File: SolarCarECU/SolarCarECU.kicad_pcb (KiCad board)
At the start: 4 copper layers, 160 x 100 mm, 116 parts, among them J1 Screw_Terminal_01x02, J2 USB_B_Micro, J3 Screw_Terminal_01x05, J4 Screw_Terminal_01x08, J5 Screw_Terminal_01x08, J6 Screw_Terminal_01x14, J7 Screw_Terminal_01x14, Q1 QM6015D, Q2 PZT2222A, Q3 QM6015D, Q4 QM6015D, Q5 QM6015D, Q6 QM6015D, U1 Teensy3.6, U10 LM324A, U2 EL7202CN, U3 EL7202CN, U4 L7805, U5 MCP2562-E-P, U6 MCP2562-E-P, U7 4504, U8 4504, U9 4504

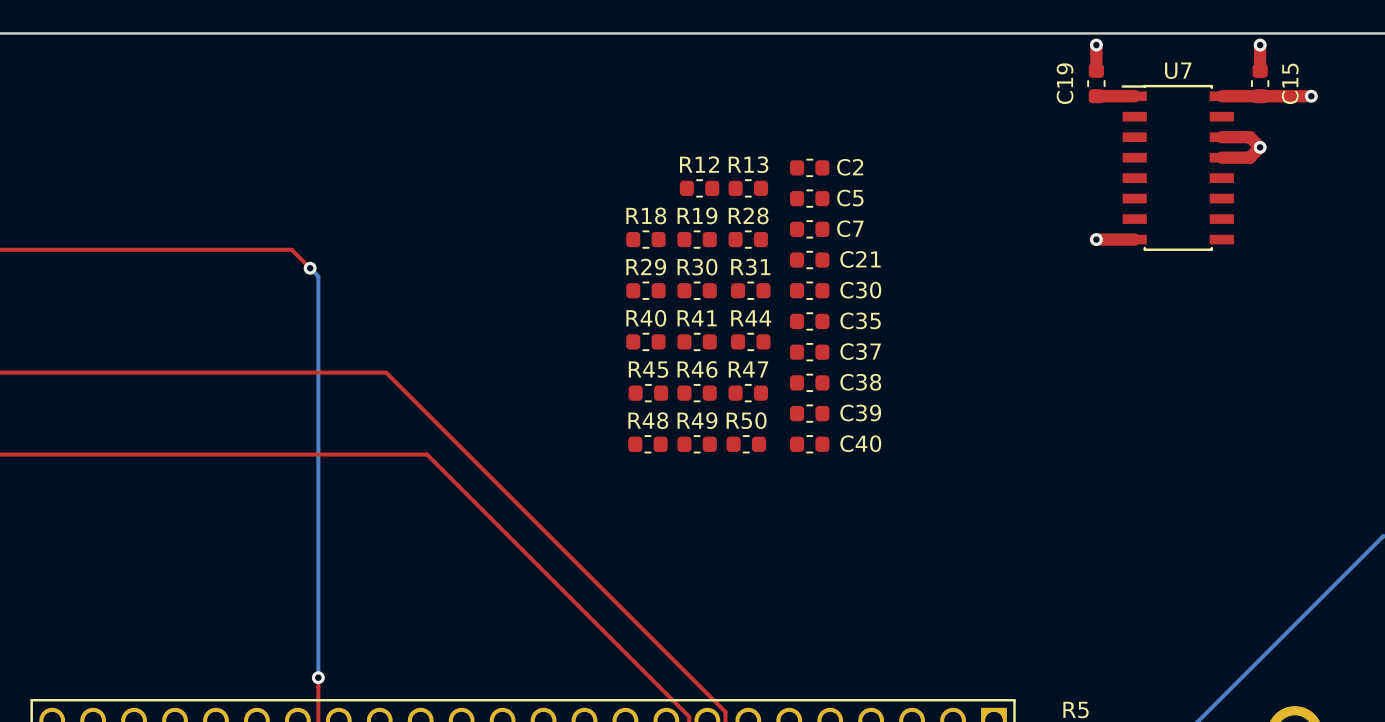
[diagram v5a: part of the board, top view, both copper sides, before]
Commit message: added logos
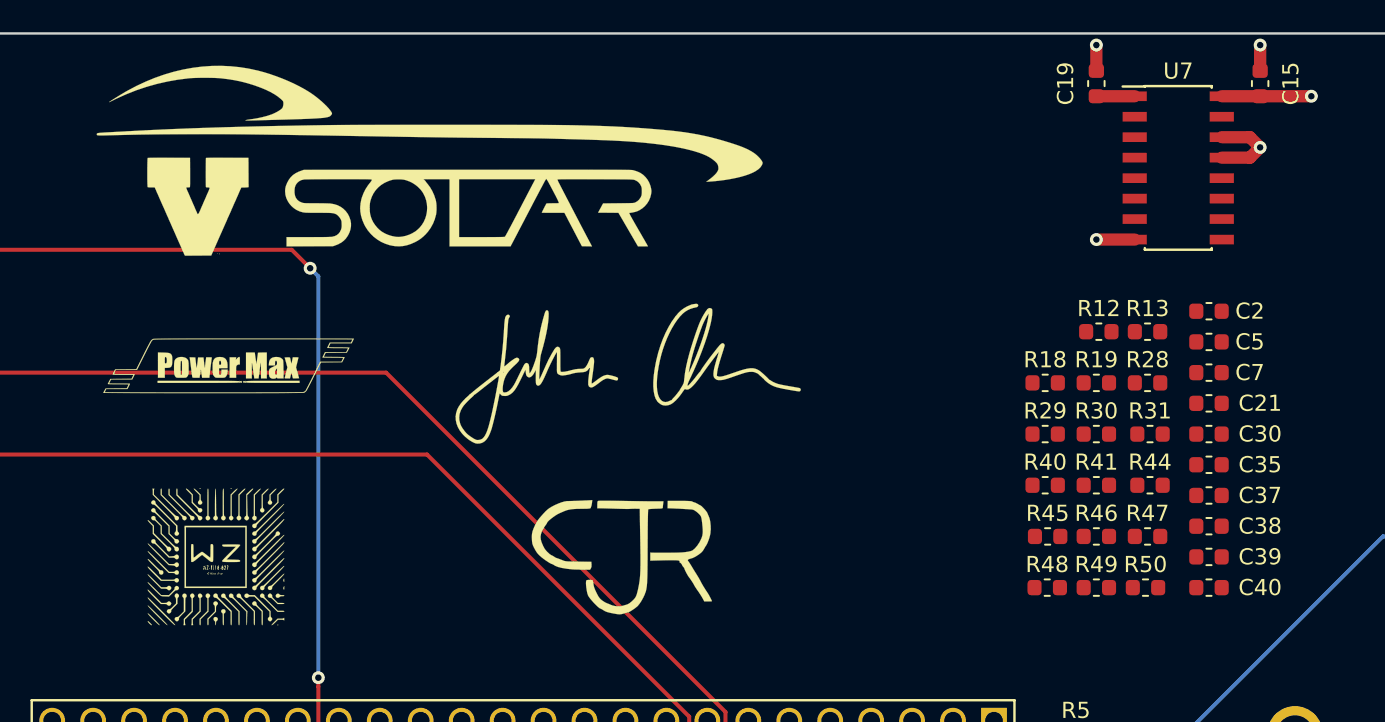
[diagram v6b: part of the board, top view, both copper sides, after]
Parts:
- added G***: LOGO, logo:SOLAR, F.Cu at (181.0, 52.7)
- added G***: LOGO, logo:PowerMax, F.Cu at (168.3, 65.4)
- added G***: LOGO, logo:WZ, F.Cu at (167.6, 77.5)
- added G***: LOGO, logo:CJR, F.Cu at (193.0, 77.5)
- added G***: LOGO, logo:JohnC, F.Cu at (192.4, 66.0)
- moved C37 26.3 mm to (229.2, 73.7)
- moved C38 26.3 mm to (229.2, 75.6)
- moved C39 26.3 mm to (229.2, 77.5)
- moved C40 26.3 mm to (229.2, 79.4)
- moved C5 26.3 mm to (229.2, 64.1)
- moved C7 26.3 mm to (229.2, 66.0)
- moved R12 26.3 mm to (222.4, 63.5)
- moved R13 26.3 mm to (225.4, 63.5)
- moved R28 26.3 mm to (225.4, 66.7)
- moved R47 26.3 mm to (225.4, 76.2)
- moved R50 26.3 mm to (225.3, 79.4)
- moved C2 26.3 mm to (229.2, 62.2)
- moved C21 26.3 mm to (229.2, 67.9)
- moved C30 26.3 mm to (229.2, 69.8)
- moved C35 26.3 mm to (229.2, 71.8)
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
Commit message: Wiring
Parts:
- moved R44 129.6 mm to (96.5, 84.5)
- moved R47 126.2 mm to (99.7, 87.0)
- moved R46 126.2 mm to (96.5, 87.0)
- moved R45 119.8 mm to (99.7, 84.5)
- moved C2 113.9 mm to (115.6, 70.2)
- moved C5 113.8 mm to (115.6, 68.6)
- moved C7 113.7 mm to (115.6, 67.0)
- moved R50 111.7 mm to (115.4, 59.1)
- moved R49 107.6 mm to (115.6, 65.4)
- moved R48 103.9 mm to (115.6, 71.8)
- moved C38 53.7 mm to (185.4, 106.7), turned to 270 degrees
- moved C37 52.9 mm to (188.0, 106.7), turned to 270 degrees
- moved C35 52.2 mm to (190.5, 106.7), turned to 270 degrees
- moved C30 51.6 mm to (193.0, 106.7), turned to 270 degrees
- moved C21 48.1 mm to (200.7, 106.7), turned to 270 degrees
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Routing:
- net /LV_MOTOR_R_METER: track 0.00 -> 134.1 mm, vias 0 -> 1
- net /LV_MOTOR_L_METER: track 0.00 -> 133.7 mm, vias 0 -> 1
- net GNDA: track 290.1 -> 323.4 mm, vias 10 -> 17
- net +12V: track 12.0 -> 24.5 mm
- net GND: track 47.3 -> 58.6 mm, vias 18 -> 20
- net Net-(Q3-Pad1): track 0.00 -> 10.1 mm
- net Net-(Q5-Pad1): track 0.00 -> 8.14 mm
- net Net-(Q4-Pad1): track 0.00 -> 7.75 mm
- net Net-(R50-Pad2): track 0.00 -> 3.41 mm
- net Net-(R49-Pad2): track 0.00 -> 3.29 mm
- net Net-(R48-Pad2): track 0.00 -> 3.29 mm
- net /MOTOR_R_METER: track 0.00 -> 3.02 mm
- net /MOTOR_L_METER: track 0.00 -> 3.02 mm
- net /LV_TURNSIG_CTRL: track 0.00 -> 3.02 mm
- net /LV_THROTTLE_CTRL: track 0.00 -> 3.02 mm
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- removed copper zone on F.Cu, net +12V
